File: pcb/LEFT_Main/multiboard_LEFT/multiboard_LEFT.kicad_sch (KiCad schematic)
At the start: 111 parts, among them SW1 RotaryEncoder_Switch, SW10 SW_Push, SW11 SW_Push, SW12 SW_Push, SW13 SW_Push, SW14 SW_Push, SW15 SW_Push, SW16 SW_Push, SW17 SW_Push, SW18 SW_Push, SW19 SW_Push, SW2 RotaryEncoder_Switch, SW20 SW_Push, SW21 SW_Push, SW22 SW_Push, SW23 SW_Push, SW24 SW_Push, SW25 SW_Push, SW26 SW_Push, SW27 SW_Push, SW28 SW_Push, SW29 SW_Push, SW3 SW_Push, SW30 SW_Push, SW31 SW_Push, SW32 SW_Push, SW33 SW_Push, SW34 SW_Push, SW35 SW_Push, SW36 SW_Push, SW37 SW_Push, SW38 SW_Push, SW39 SW_Push, SW4 SW_Push, SW40 SW_Push, SW41 SW_Push, SW42 SW_Push, SW46 SW_Push, SW47 SW_Push, SW48 SW_Push, SW49 SW_Push, SW5 SW_Push, SW50 SW_Push, SW51 SW_Push, SW52 SW_Push, SW56 SW_Push, SW57 SW_Push, SW58 SW_Push, SW59 SW_Push, SW6 SW_Push, SW60 SW_Push, SW61 SW_Push, SW62 SW_Push, SW7 SW_Push, SW8 SW_Push, SW9 SW_Push, U1 ESP32-S3-DEVKITC-1-N8R2

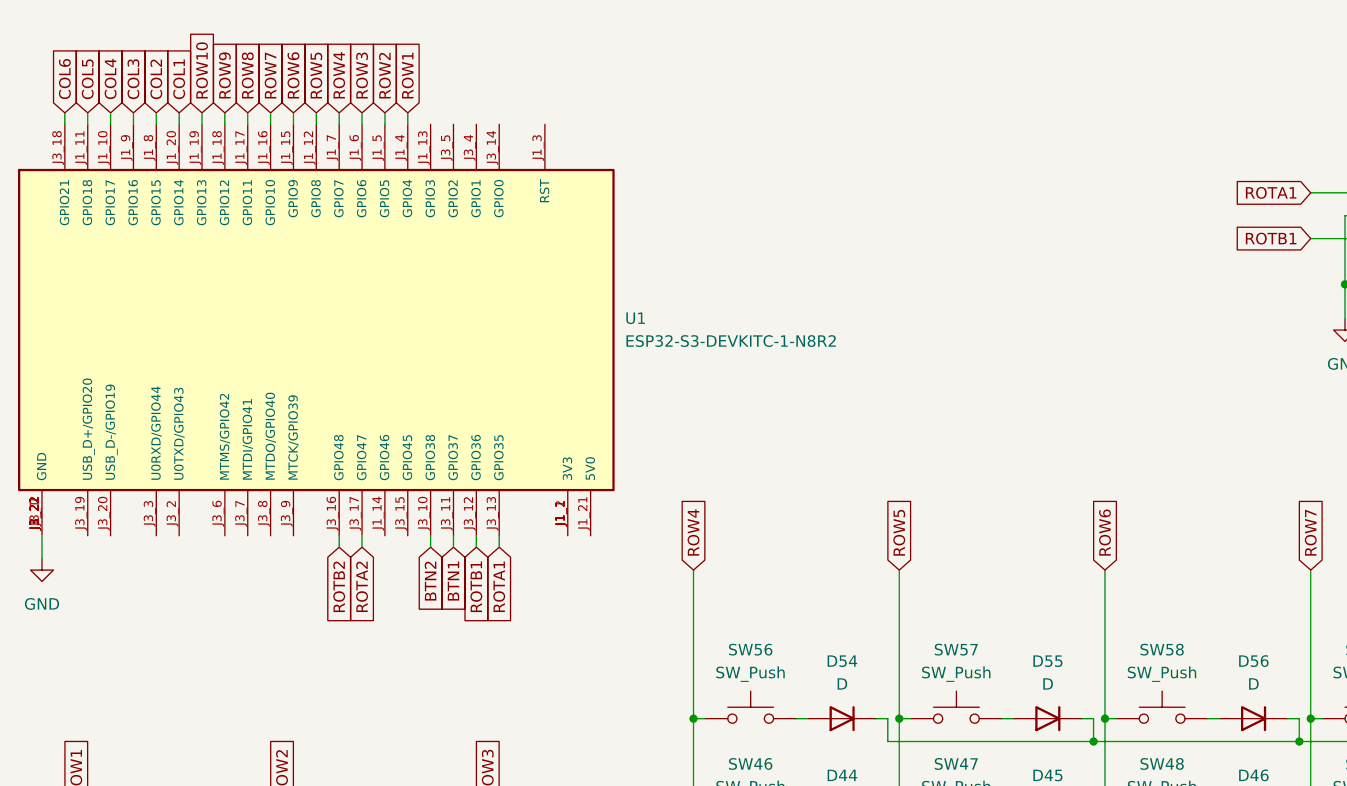
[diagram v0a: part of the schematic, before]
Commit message: add headphone jack
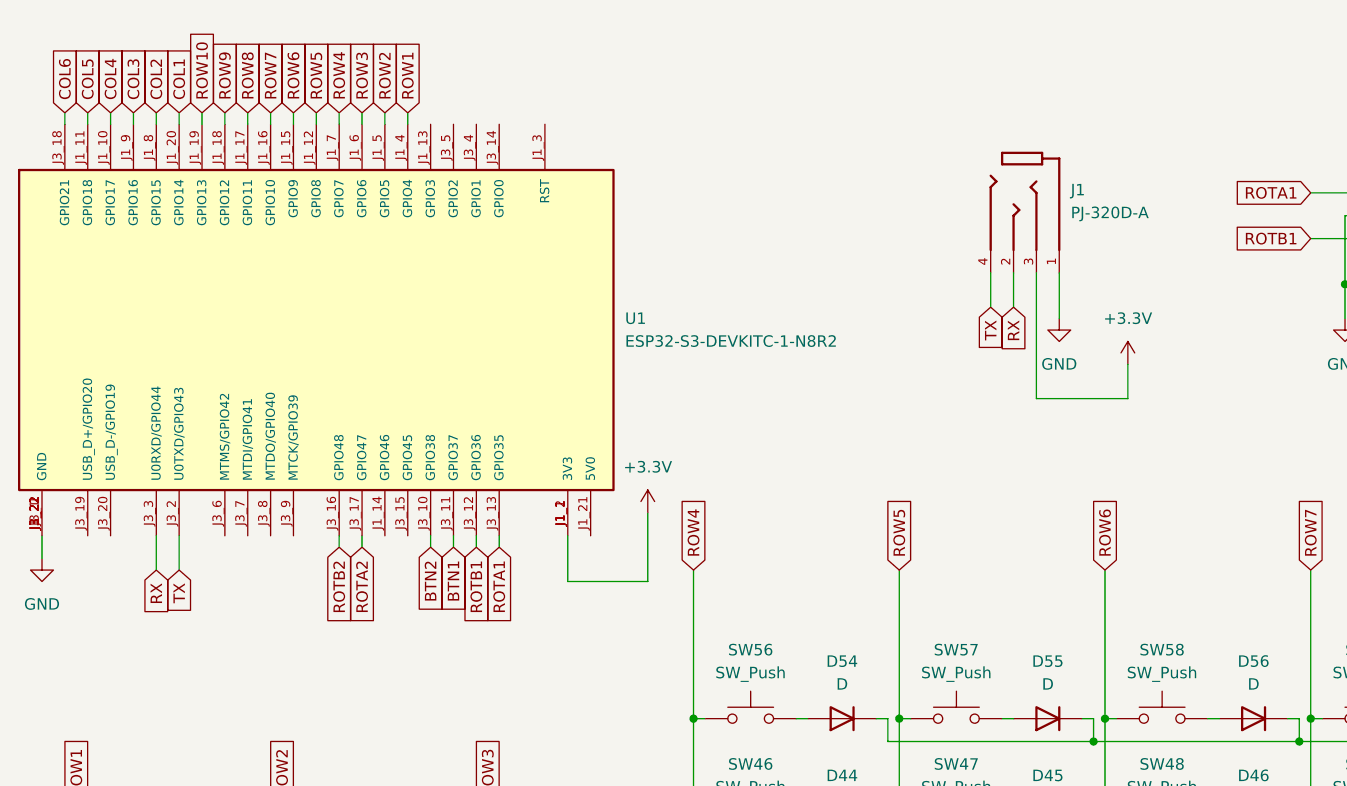
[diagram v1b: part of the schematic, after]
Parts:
- added J1: PJ-320D-A, PJ:HRO_PJ-320D-A, symbol PJ:PJ-320D-A
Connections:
- net GND: now also J1.1
- net +3.3V: now reaches U1.J1_1 (3V3), U1.J1_2 (3V3)
- net +3.3V: now also J1.3
- net TX: now reaches U1.J3_2 (U0TXD/GPIO43)
- net TX: now also J1.4
- net RX: now reaches U1.J3_3 (U0RXD/GPIO44)
- net RX: now also J1.2
